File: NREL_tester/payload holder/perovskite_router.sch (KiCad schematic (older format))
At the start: 3 parts, among them J1 Conn_01x10_Male, J2 Conn_01x10_Male, J3 Conn_01x11_Male

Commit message: Flight computer v2 complete
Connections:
- net COMMON_1: now also J3.11 (Pin_11); no longer J3.9 (Pin_9)
- net GND: now also J3.10 (Pin_10); no longer J3.8 (Pin_8)
- net SCL: now also J3.9 (Pin_9); no longer J3.10 (Pin_10)
- net SDA: now also J3.8 (Pin_8); no longer J3.11 (Pin_11)
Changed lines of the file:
@@
 L power:GND #PWR0106
 U 1 1 64AB952A
-P 4850 4800
-F 0 "#PWR0106" H 4850 4550 50  0001 C CNN
-F 1 "GND" H 4855 4627 50  0000 C CNN
-F 2 "" H 4850 4800 50  0001 C CNN
-F 3 "" H 4850 4800 50  0001 C CNN
-	1    4850 4800
+P 4850 5000
+F 0 "#PWR0106" H 4850 4750 50  0001 C CNN
+F 1 "GND" H 4855 4827 50  0000 C CNN
+F 2 "" H 4850 5000 50  0001 C CNN
+F 3 "" H 4850 5000 50  0001 C CNN
+	1    4850 5000
 	1    0    0    -1
 $EndComp
-Text GLabel 4600 4700 2    50   Input ~ 0
+Text GLabel 4600 4400 2    50   Input ~ 0
 SDA
-Text GLabel 4600 4600 2    50   Input ~ 0
+Text GLabel 4600 4500 2    50   Input ~ 0
 SCL
 Text GLabel 4600 4200 2    50   Input ~ 0
@@
 Text GLabel 4600 3700 2    50   Input ~ 0
 CELL_4
-Text GLabel 5450 4450 2    50   Input ~ 0
+Text GLabel 5450 4650 2    50   Input ~ 0
 COMMON_1
-Text GLabel 5450 4550 2    50   Input ~ 0
+Text GLabel 5450 4750 2    50   Input ~ 0
 COMMON_2
 $Comp
@@
 $EndComp
 Wire Wire Line
-	5450 4450 5400 4450
+	5450 4650 5400 4650
 Wire Wire Line
-	5400 4450 5400 4500
+	5400 4650 5400 4700
 Wire Wire Line
-	5400 4550 5450 4550
+	5400 4750 5450 4750
 Wire Wire Line
-	5400 4500 4600 4500
-Connection ~ 5400 4500
+	5400 4700 4600 4700
+Connection ~ 5400 4700
 Wire Wire Line
-	5400 4500 5400 4550
+	5400 4700 5400 4750
 Wire Wire Line
-	4600 4400 4850 4400
+	4600 4600 4850 4600
 Wire Wire Line
-	4850 4400 4850 4800
+	4850 4600 4850 5000
 Wire Wire Line
 	4600 4300 5050 4300

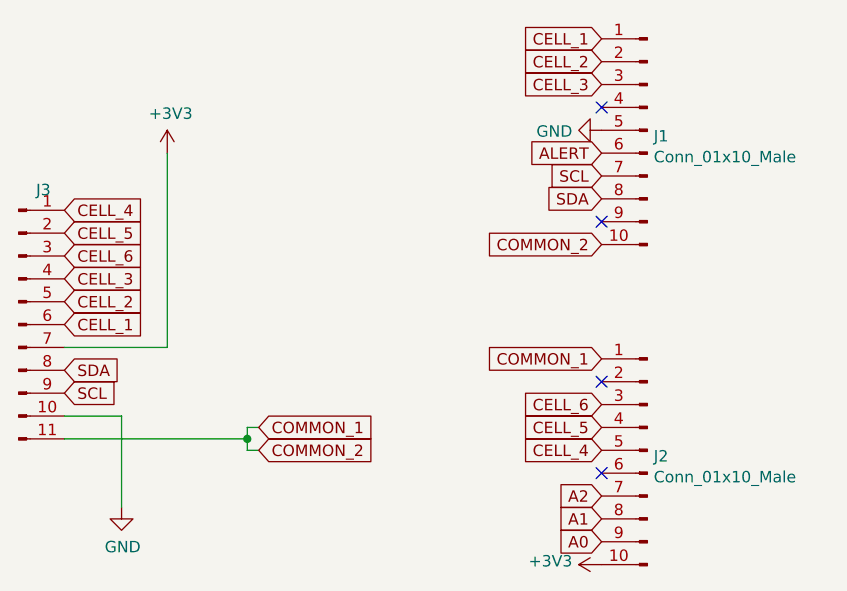
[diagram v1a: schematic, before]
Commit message: Update hardware
- Add separate discharge resistance paths to flight computer
- Update footprint for payload holder
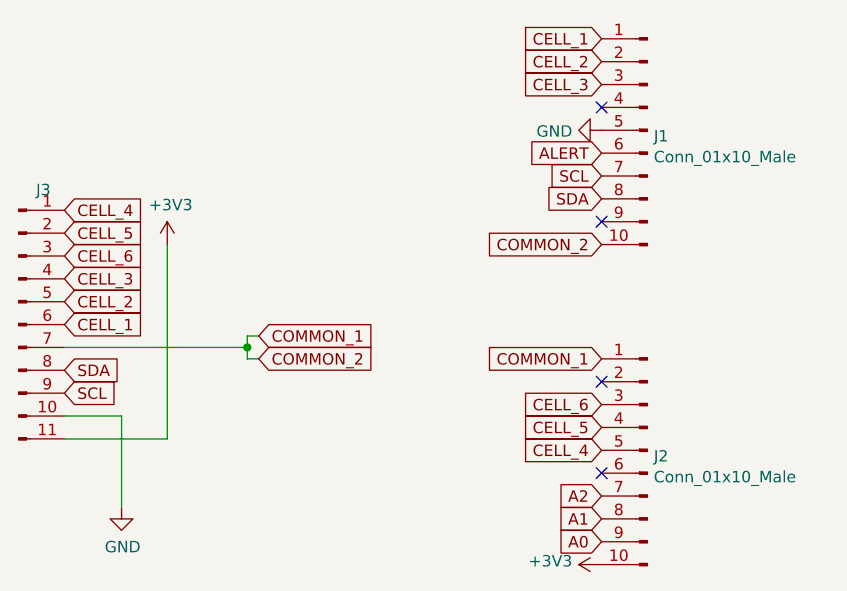
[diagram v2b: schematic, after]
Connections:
- net +3V3: now also J3.11 (Pin_11); no longer J3.7 (Pin_7)
- net COMMON_1: now also J3.7 (Pin_7); no longer J3.11 (Pin_11)
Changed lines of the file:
@@
 L power:+3V3 #PWR0105
 U 1 1 64AB8FC1
-P 5050 3450
-F 0 "#PWR0105" H 5050 3300 50  0001 C CNN
-F 1 "+3V3" H 5065 3623 50  0000 C CNN
-F 2 "" H 5050 3450 50  0001 C CNN
-F 3 "" H 5050 3450 50  0001 C CNN
-	1    5050 3450
+P 5050 3850
+F 0 "#PWR0105" H 5050 3700 50  0001 C CNN
+F 1 "+3V3" H 5065 4023 50  0000 C CNN
+F 2 "" H 5050 3850 50  0001 C CNN
+F 3 "" H 5050 3850 50  0001 C CNN
+	1    5050 3850
 	1    0    0    -1
 $EndComp
@@
 Text GLabel 4600 3700 2    50   Input ~ 0
 CELL_4
-Text GLabel 5450 4650 2    50   Input ~ 0
+Text GLabel 5450 4250 2    50   Input ~ 0
 COMMON_1
-Text GLabel 5450 4750 2    50   Input ~ 0
+Text GLabel 5450 4350 2    50   Input ~ 0
 COMMON_2
 $Comp
@@
 $EndComp
 Wire Wire Line
-	5450 4650 5400 4650
+	5450 4250 5400 4250
 Wire Wire Line
-	5400 4650 5400 4700
+	5400 4250 5400 4300
 Wire Wire Line
-	5400 4750 5450 4750
+	5400 4350 5450 4350
 Wire Wire Line
-	5400 4700 4600 4700
-Connection ~ 5400 4700
+	5400 4300 4600 4300
+Connection ~ 5400 4300
 Wire Wire Line
-	5400 4700 5400 4750
+	5400 4300 5400 4350
 Wire Wire Line
 	4600 4600 4850 4600
@@
 	4850 4600 4850 5000
 Wire Wire Line
-	4600 4300 5050 4300
+	4600 4700 5050 4700
 Wire Wire Line
-	5050 4300 5050 3450
+	5050 4700 5050 3850
 $EndSCHEMATC
